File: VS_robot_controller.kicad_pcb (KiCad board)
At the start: 2 copper layers, 70.5 x 67 mm, 11 parts, among them U1 NRF24L01_Breakout

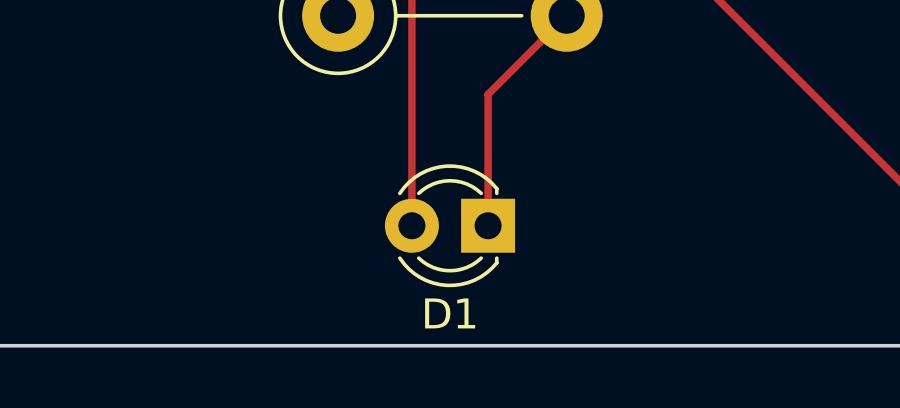
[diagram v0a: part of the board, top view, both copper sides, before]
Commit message: Added README and modified LED label
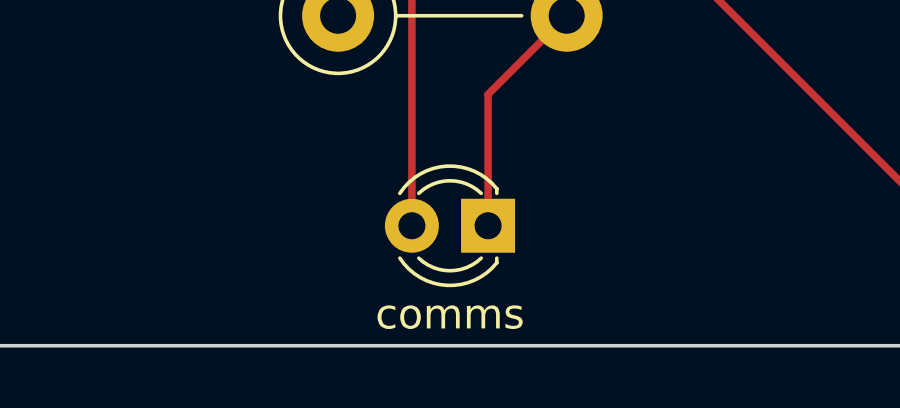
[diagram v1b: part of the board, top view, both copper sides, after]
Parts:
- renumbered D1 to comms
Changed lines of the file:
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@@
     (descr "LED, diameter 3.0mm, 2 pins")
     (tags "LED diameter 3.0mm 2 pins")
-    (fp_text reference D1 (at 1.27 -2.96) (layer F.SilkS)
+    (fp_text reference comms (at 1.27 -2.96) (layer F.SilkS)
       (effects (font (size 1 1) (thickness 0.15)))
     )

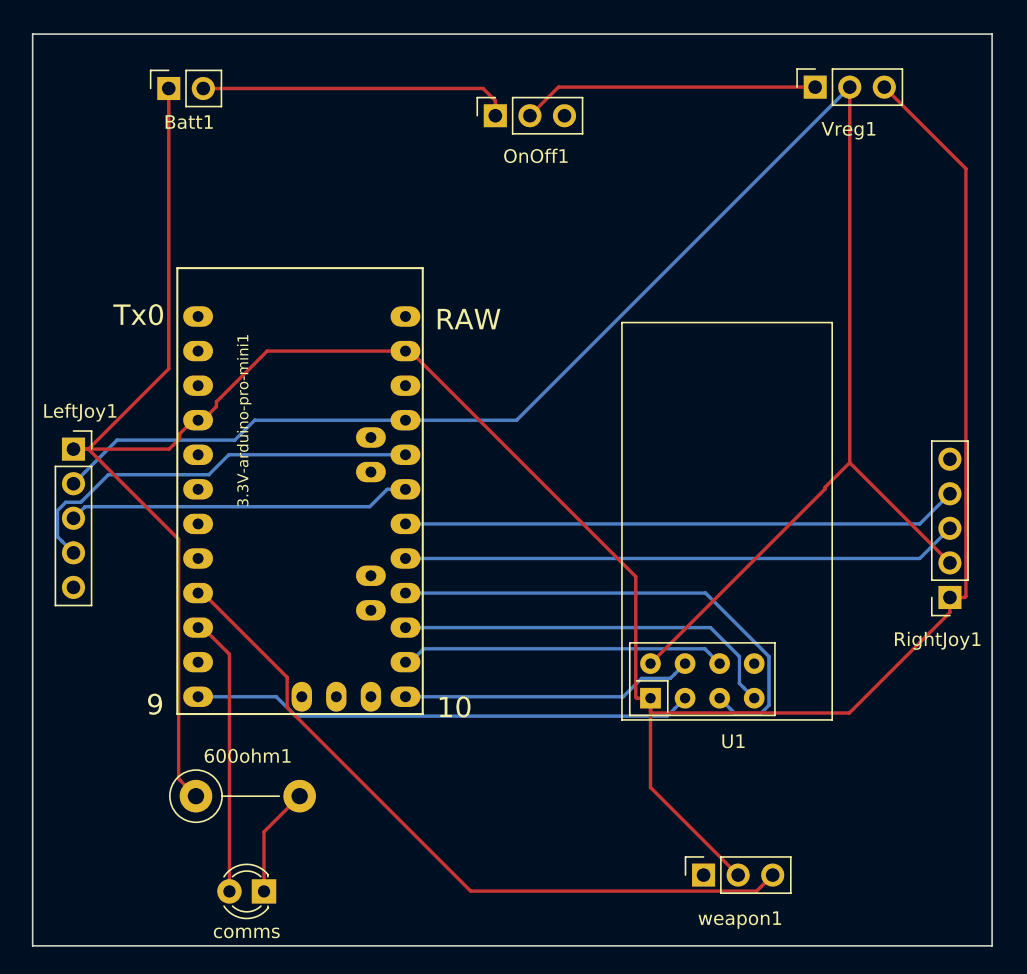
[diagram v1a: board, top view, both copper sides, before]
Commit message: joysticks were wired backwards. fixed
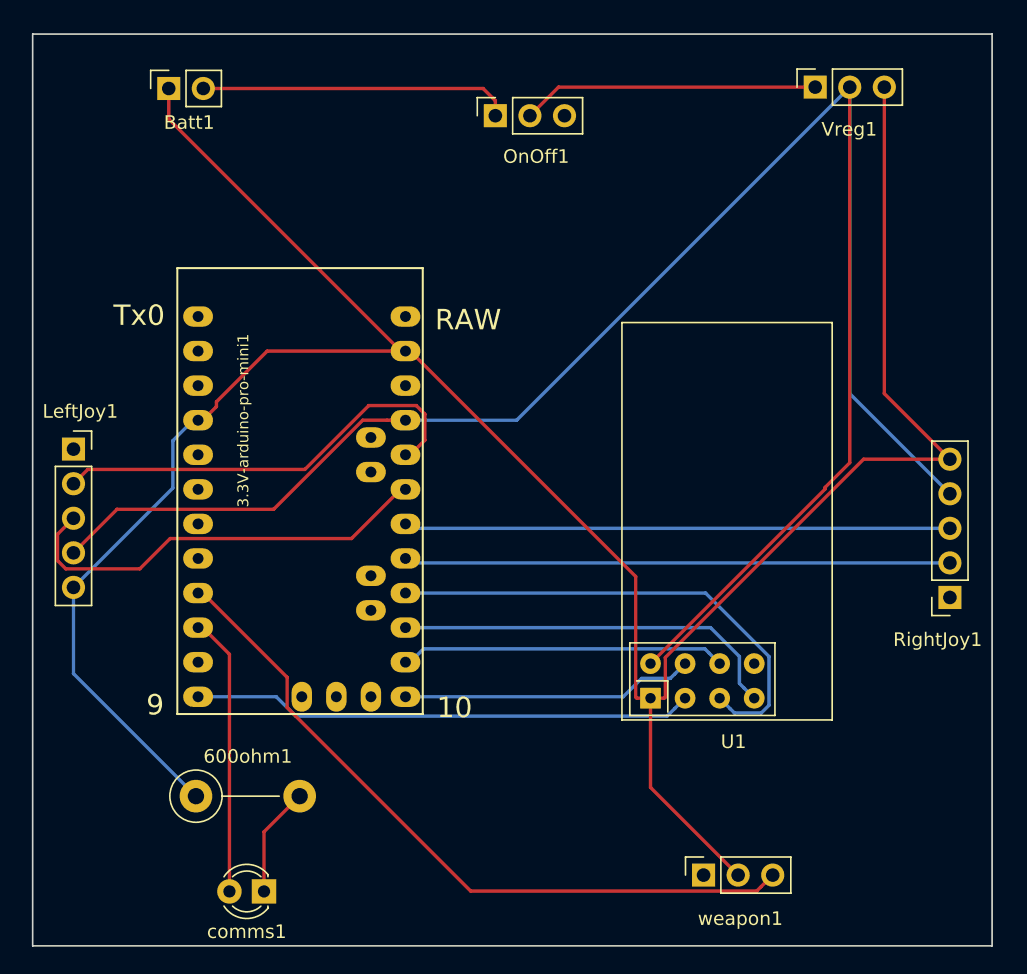
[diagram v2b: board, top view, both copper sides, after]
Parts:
- moved G*** 2.06 mm to (206.3, 86.9)
- renumbered comms to comms1
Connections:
- LeftJoy1 pad 1: GND -> Net-(LeftJoy1-Pad1)
- LeftJoy1 pad 2: +3V3 -> Net-(3.3V-arduino-pro-mini1-Pad20)
- LeftJoy1 pad 4: Net-(3.3V-arduino-pro-mini1-Pad20) -> +3V3
- LeftJoy1 pad 5: Net-(LeftJoy1-Pad5) -> GND
- RightJoy1 pad 1: GND -> Net-(RightJoy1-Pad1)
- RightJoy1 pad 2: +3V3 -> Net-(3.3V-arduino-pro-mini1-Pad17)
- RightJoy1 pad 3: Net-(3.3V-arduino-pro-mini1-Pad17) -> Net-(3.3V-arduino-pro-mini1-Pad18)
- RightJoy1 pad 4: Net-(3.3V-arduino-pro-mini1-Pad18) -> +3V3
- RightJoy1 pad 5: Net-(RightJoy1-Pad5) -> GND
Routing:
- net +3V3: track 127.9 -> 152.6 mm
- net GND: track 204.3 -> 189.3 mm
- net Net-(3.3V-arduino-pro-mini1-Pad19): track 25.3 -> 31.8 mm
- net Net-(3.3V-arduino-pro-mini1-Pad20): track 30.9 -> 32.2 mm
- net Net-(3.3V-arduino-pro-mini1-Pad18): track 40.9 -> 40.1 mm
- net Net-(3.3V-arduino-pro-mini1-Pad17): track 40.9 -> 40.1 mm

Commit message: cleaned up silk screen labels, added polarity indication
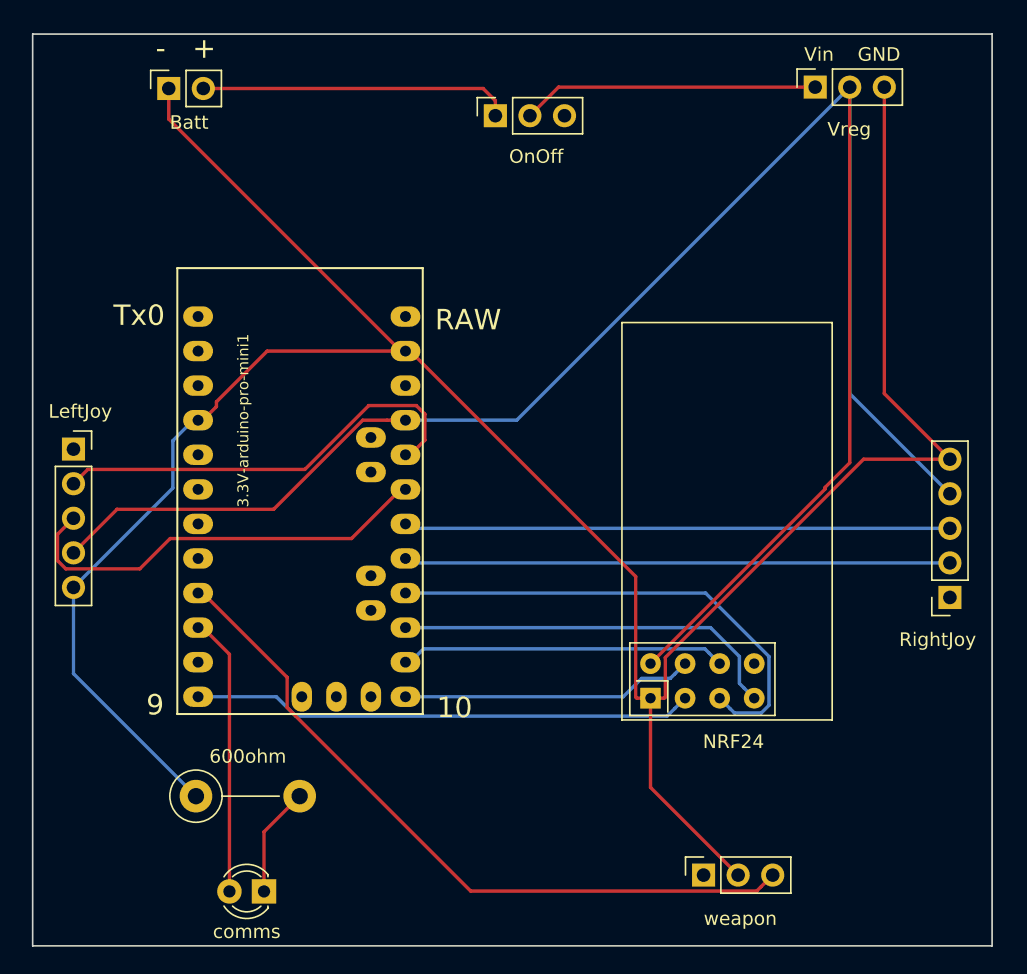
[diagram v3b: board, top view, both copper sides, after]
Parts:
- renumbered 600ohm1 to 600ohm, Batt1 to Batt, LeftJoy1 to LeftJoy, U1 to NRF24, OnOff1 to OnOff, RightJoy1 to RightJoy, Vreg1 to Vreg, comms1 to comms, weapon1 to weapon
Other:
- board text added: "- +"
- board text added: "Vin GND"
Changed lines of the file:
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@@
   (general
     (thickness 1.6)
-    (drawings 10)
+    (drawings 12)
     (tracks 105)
     (zones 0)
@@
     (descr "nRF24L01 breakout board")
     (tags "nRF24L01 adapter breakout")
-    (fp_text reference U1 (at -3.2 6.1 180) (layer F.SilkS)
+    (fp_text reference NRF24 (at -3.2 6.1 180) (layer F.SilkS)
       (effects (font (size 1 1) (thickness 0.15)))
     )
@@
     (descr "Through hole straight socket strip, 1x05, 2.54mm pitch, single row (from Kicad 4.0.7), script generated")
     (tags "Through hole socket strip THT 1x05 2.54mm single row")
-    (fp_text reference RightJoy1 (at 0.9 -3.1) (layer F.SilkS)
+    (fp_text reference RightJoy (at 0.9 -3.1) (layer F.SilkS)
       (effects (font (size 1 1) (thickness 0.15)))
     )
@@
     (descr "LED, diameter 3.0mm, 2 pins")
     (tags "LED diameter 3.0mm 2 pins")
-    (fp_text reference comms1 (at 1.27 -2.96) (layer F.SilkS)
+    (fp_text reference comms (at 1.27 -2.96) (layer F.SilkS)
       (effects (font (size 1 1) (thickness 0.15)))
     )
@@
     (descr "Through hole straight socket strip, 1x05, 2.54mm pitch, single row (from Kicad 4.0.7), script generated")
     (tags "Through hole socket strip THT 1x05 2.54mm single row")
-    (fp_text reference LeftJoy1 (at 0.5 -2.77) (layer F.SilkS)
+    (fp_text reference LeftJoy (at 0.5 -2.77) (layer F.SilkS)
       (effects (font (size 1 1) (thickness 0.15)))
     )
@@
     (descr "Through hole straight socket strip, 1x03, 2.54mm pitch, single row (from Kicad 4.0.7), script generated")
     (tags "Through hole socket strip THT 1x03 2.54mm single row")
-    (fp_text reference Vreg1 (at -3.1 2.5 180) (layer F.SilkS)
+    (fp_text reference Vreg (at -3.1 2.5 180) (layer F.SilkS)
       (effects (font (size 1 1) (thickness 0.15)))
     )
@@
     (descr "Resistor, Axial_DIN0411 series, Axial, Vertical, pin pitch=7.62mm, 1W, length*diameter=9.9*3.6mm^2")
     (tags "Resistor Axial_DIN0411 series Axial Vertical pin pitch 7.62mm 1W length 9.9mm diameter 3.6mm")
-    (fp_text reference 600ohm1 (at 3.81 -2.92) (layer F.SilkS)
+    (fp_text reference 600ohm (at 3.81 -2.92) (layer F.SilkS)
       (effects (font (size 1 1) (thickness 0.15)))
     )
@@
     (descr "Through hole straight socket strip, 1x03, 2.54mm pitch, single row (from Kicad 4.0.7), script generated")
     (tags "Through hole socket strip THT 1x03 2.54mm single row")
-    (fp_text reference OnOff1 (at -3 3 180) (layer F.SilkS)
+    (fp_text reference OnOff (at -3 3 180) (layer F.SilkS)
       (effects (font (size 1 1) (thickness 0.15)))
     )
@@
     (descr "Through hole straight socket strip, 1x03, 2.54mm pitch, single row (from Kicad 4.0.7), script generated")
     (tags "Through hole socket strip THT 1x03 2.54mm single row")
-    (fp_text reference weapon1 (at -3.2 2.7 180) (layer F.SilkS)
+    (fp_text reference weapon (at -3.2 2.7 180) (layer F.SilkS)
       (effects (font (size 1 1) (thickness 0.15)))
     )
@@
     (descr "Through hole straight socket strip, 1x02, 2.54mm pitch, single row (from Kicad 4.0.7), script generated")
     (tags "Through hole socket strip THT 1x02 2.54mm single row")
-    (fp_text reference Batt1 (at -2.5 1.5 180) (layer F.SilkS)
+    (fp_text reference Batt (at -2.5 1.5 180) (layer F.SilkS)
       (effects (font (size 1 1) (thickness 0.15)))
     )
@@
     )
   )
+  (gr_text "Vin    GND" (at 230.725 41.5) (layer F.SilkS)
+    (effects (font (size 1 1) (thickness 0.25)))
+  )
+  (gr_text "-   +" (at 181.75 41.05) (layer F.SilkS)
+    (effects (font (size 1.5 1.5) (thickness 0.3)))
+  )
   (gr_text V1 (at 206.1 55.575) (layer B.SilkS)

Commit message: moved joysticks up
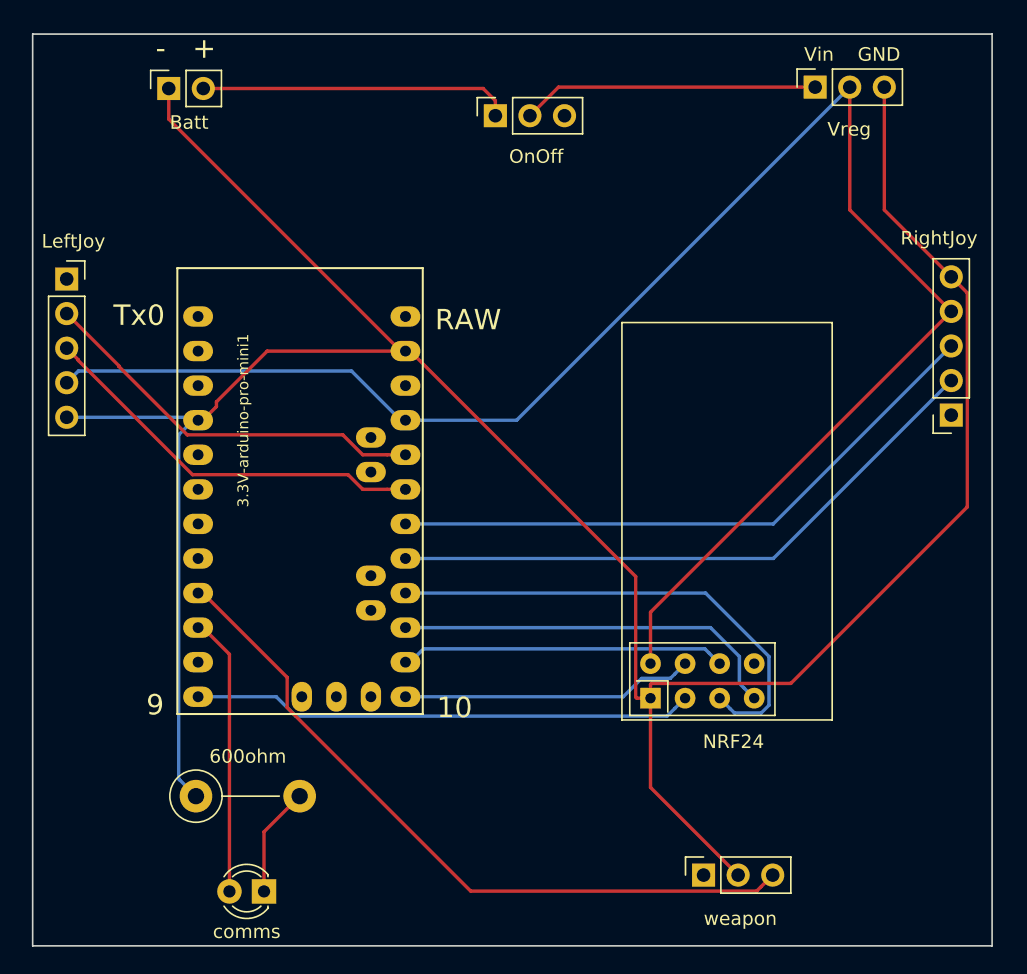
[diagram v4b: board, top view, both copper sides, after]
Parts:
- moved RightJoy 13.4 mm to (238.0, 68.0)
- moved LeftJoy 12.5 mm to (173.0, 58.0)
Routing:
- net +3V3: track 152.6 -> 124.1 mm
- net GND: track 189.3 -> 195.4 mm
- net Net-(3.3V-arduino-pro-mini1-Pad18): track 40.1 -> 46.0 mm
- net Net-(3.3V-arduino-pro-mini1-Pad17): track 40.1 -> 45.5 mm
- net Net-(3.3V-arduino-pro-mini1-Pad20): track 32.2 -> 29.2 mm
- net Net-(3.3V-arduino-pro-mini1-Pad19): track 31.8 -> 29.2 mm
